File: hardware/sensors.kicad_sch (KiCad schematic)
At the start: 15 parts, among them U3 LIS3DH, U4 IMP23ABSU, U5 TMP102xxDRL, U6 VCNL_4020

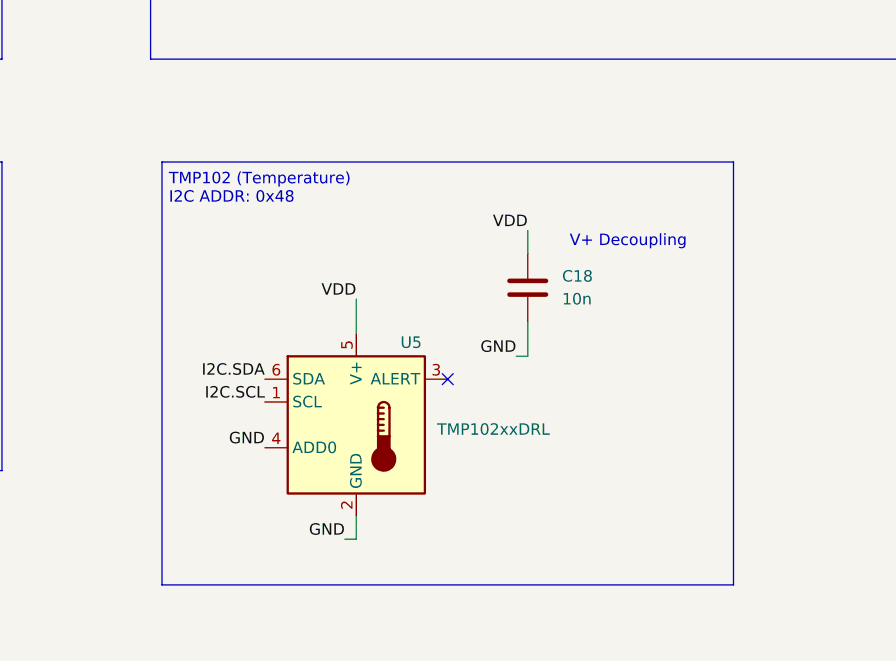
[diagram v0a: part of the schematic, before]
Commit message: [Hardware] Remove tmp102
No longer using the tmp102 temperature sensor, so remove it from the board.
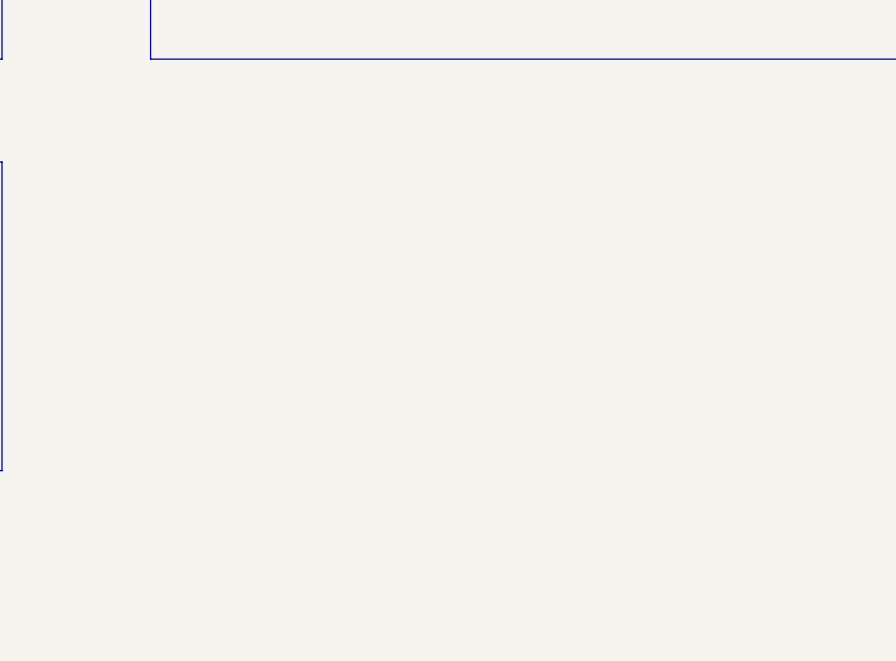
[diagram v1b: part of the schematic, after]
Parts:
- removed C18: 10n, Capacitor_SMD:C_0603_1608Metric_Pad1.08x0.95mm_HandSolder, symbol Device:C
- removed U5: TMP102xxDRL, Package_TO_SOT_SMD:SOT-563, symbol Sensor_Temperature:TMP102xxDRL
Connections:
- no-connect marks 6 -> 5
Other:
- note removed: "TMP102 (Temperature) I2C ADDR: 0x48"
- note removed: "V+ Decoupling"

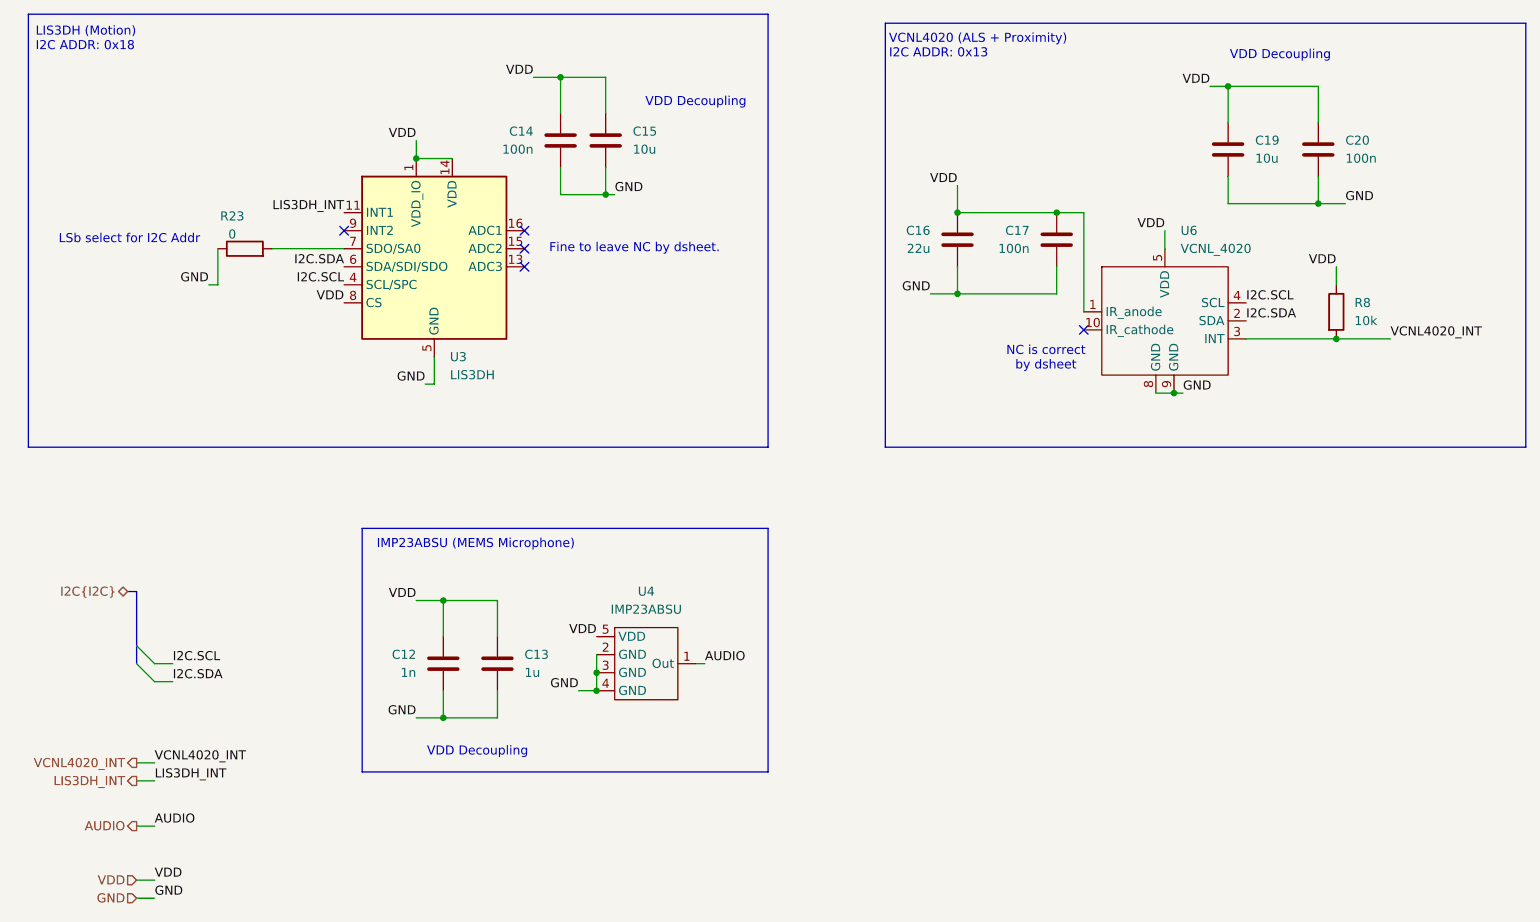
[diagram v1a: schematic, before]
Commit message: [Hardware] Replace LISDH Motion Sensor with LSM6DSM
Change motion sensor to an accelerometer + gyro unit. Route the second interrupt line to the STM32.
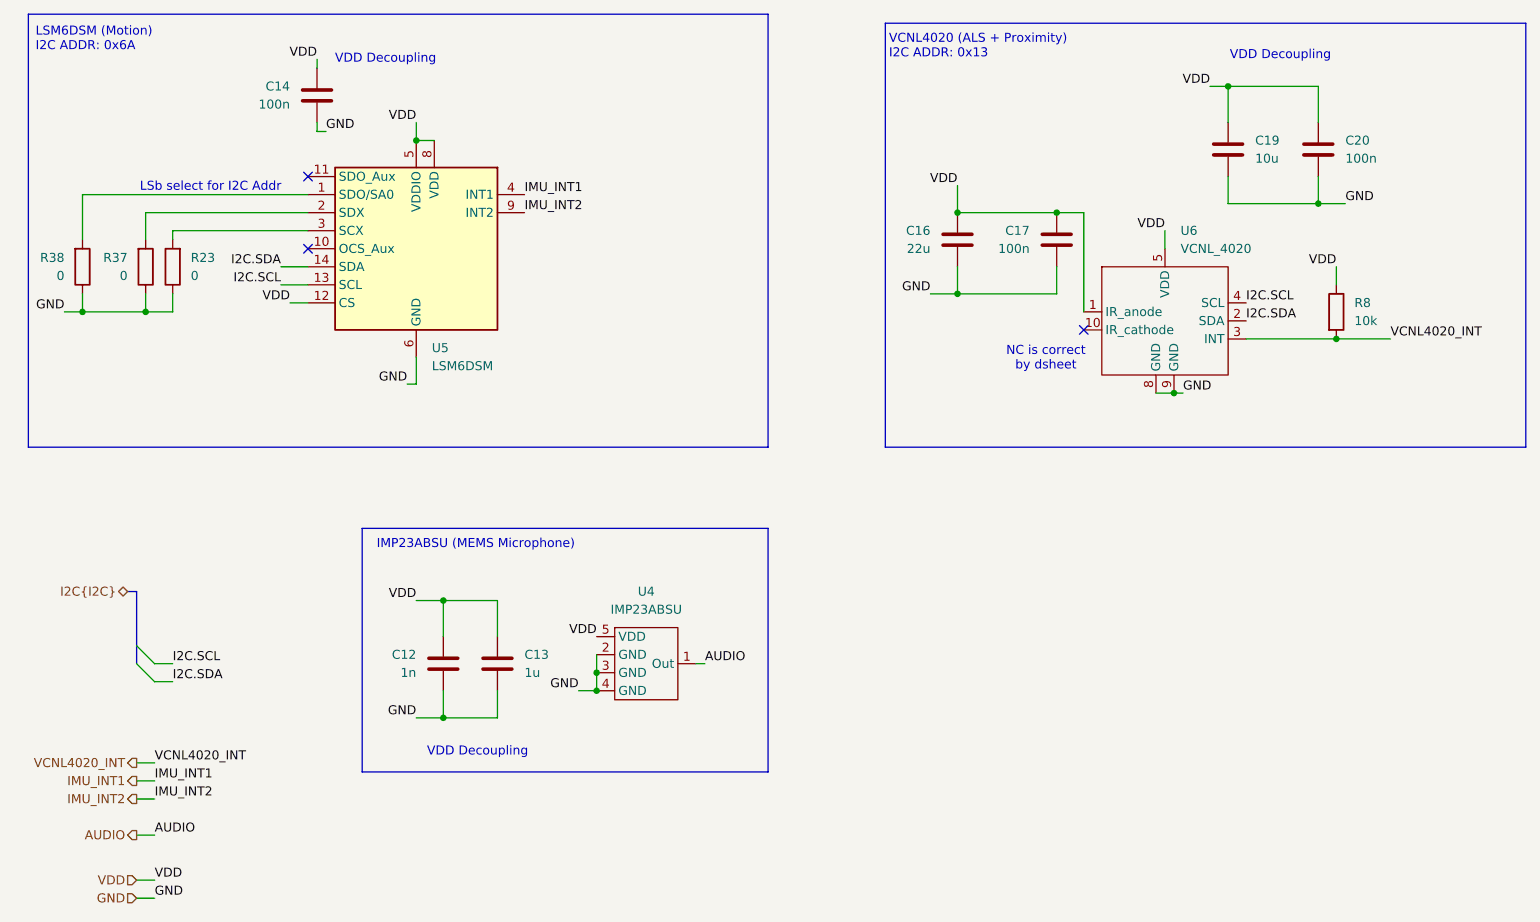
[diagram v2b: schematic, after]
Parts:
- removed C15: 10u, Capacitor_SMD:C_0603_1608Metric_Pad1.08x0.95mm_HandSolder, symbol Device:C
- removed U3: LIS3DH, Package_LGA:LGA-16_3x3mm_P0.5mm_LayoutBorder3x5y, symbol Sensor_Motion:LIS3DH
- added R37, R38: 0, Resistor_SMD:R_0603_1608Metric_Pad0.98x0.95mm_HandSolder, symbol Device:R
- added U5: LSM6DSM, Package_LGA:LGA-14_3x2.5mm_P0.5mm_LayoutBorder3x4y, symbol Sensor_Motion:LSM6DSM
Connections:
- net GND: now also R37.1, R38.1, U5.6 (GND), U5.7 (GND)
- net I2C.SCL: now also U5.13 (SCL)
- net I2C.SDA: now also U5.14 (SDA)
- net VDD: now also U5.12 (CS), U5.5 (VDDIO), U5.8 (VDD)
- net at R23.2: now also U5.3 (SCX)
- new net: R38.2, U5.1 (SDO/SA0)
- new net: R37.2, U5.2 (SDX)
- new net IMU_INT1: U5.4 (INT1)
- new net IMU_INT2: U5.9 (INT2)
- no-connect marks 5 -> 3
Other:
- note added: "LSM6DSM (Motion) I2C ADDR: 0x6A"
- note removed: "Fine to leave NC by dsheet."
- note removed: "LIS3DH (Motion) I2C ADDR: 0x18"
- moved on the sheet: C14

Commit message: Change many passives to 0402 and assign part numbers
Incorporate 0402 parts where possible
Assign Manufacturer Part Numbers to parts where possible
Update layout for the new passive sizes
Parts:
- C12: footprint Capacitor_SMD:C_0603_1608Metric_Pad1.08x0.95mm_HandSolder -> Capacitor_SMD:C_0402_1005Metric; MPN (none) -> C0402C102K4RACTU
- C13: MPN (none) -> CL05A105KO5NNNC
- C14, C17, C20: footprint Capacitor_SMD:C_0603_1608Metric_Pad1.08x0.95mm_HandSolder -> Capacitor_SMD:C_0402_1005Metric; MPN (none) -> CL05A104KA5NNNC
- C16: MPN (none) -> CL10A226MO7JZNC
- C19: MPN (none) -> CL10A106MQ8NNNC
- R23, R37, R38: footprint Resistor_SMD:R_0603_1608Metric_Pad0.98x0.95mm_HandSolder -> Resistor_SMD:R_0402_1005Metric; MPN (none) -> RC0402JR-070RL
- R8: footprint Resistor_SMD:R_0603_1608Metric_Pad0.98x0.95mm_HandSolder -> Resistor_SMD:R_0402_1005Metric; MPN (none) -> RC0402FR-0710KL
- U4: MPN (none) -> IMP23ABSUTR
- U5: MPN (none) -> LSM6DSMTR
- U6: MPN (none) -> VCNL4020-GS08
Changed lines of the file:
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@@
 			)
 		)
-		(property "Footprint" "Capacitor_SMD:C_0603_1608Metric_Pad1.08x0.95mm_HandSolder"
+		(property "Footprint" "Capacitor_SMD:C_0402_1005Metric"
 			(at 175.5648 52.07 0)
 			(effects
@@
 		)
 		(property "Description" "Unpolarized capacitor"
+			(at 176.53 48.26 0)
+			(effects
+				(font
+					(size 1.27 1.27)
+				)
+				(hide yes)
+			)
+		)
+		(property "MPN" "CL05A104KA5NNNC"
 			(at 176.53 48.26 0)
 			(effects
@@
 			)
 		)
-		(property "Footprint" "Resistor_SMD:R_0603_1608Metric_Pad0.98x0.95mm_HandSolder"
+		(property "Footprint" "Resistor_SMD:R_0402_1005Metric"
 			(at 53.848 52.07 90)
 			(effects
@@
 		)
 		(property "Description" "Resistor"
+			(at 52.07 52.07 0)
+			(effects
+				(font
+					(size 1.27 1.27)
+				)
+				(hide yes)
+			)
+		)
+		(property "MPN" "RC0402JR-070RL"
 			(at 52.07 52.07 0)
 			(effects
@@
 			)
 		)
-		(property "Footprint" "Capacitor_SMD:C_0603_1608Metric_Pad1.08x0.95mm_HandSolder"
+		(property "Footprint" "Capacitor_SMD:C_0402_1005Metric"
 			(at 71.4248 31.75 0)
 			(effects
@@
 		)
 		(property "Description" "Unpolarized capacitor"
+			(at 72.39 27.94 0)
+			(effects
+				(font
+					(size 1.27 1.27)
+				)
+				(hide yes)
+			)
+		)
+		(property "MPN" "CL05A104KA5NNNC"
 			(at 72.39 27.94 0)
 			(effects
@@
 			)
 		)
+		(property "MPN" "CL10A106MQ8NNNC"
+			(at 200.66 35.56 0)
+			(effects
+				(font
+					(size 1.27 1.27)
+				)
+				(hide yes)
+			)
+		)
 		(pin "2"
 		)
@@
 			)
 		)
-		(property "Footprint" "Resistor_SMD:R_0603_1608Metric_Pad0.98x0.95mm_HandSolder"
+		(property "Footprint" "Resistor_SMD:R_0402_1005Metric"
 			(at 37.592 52.07 90)
 			(effects
@@
 			)
 		)
+		(property "MPN" "RC0402JR-070RL"
+			(at 39.37 52.07 0)
+			(effects
+				(font
+					(size 1.27 1.27)
+				)
+				(hide yes)
+			)
+		)
 		(pin "1"
 		)
@@
 			)
 		)
-		(property "Footprint" "Capacitor_SMD:C_0603_1608Metric_Pad1.08x0.95mm_HandSolder"
+		(property "Footprint" "Capacitor_SMD:C_0402_1005Metric"
 			(at 91.1352 111.76 0)
 			(effects
@@
 		)
 		(property "Description" "Unpolarized capacitor"
+			(at 90.17 107.95 0)
+			(effects
+				(font
+					(size 1.27 1.27)
+				)
+				(hide yes)
+			)
+		)
+		(property "MPN" "C0402C102K4RACTU"
 			(at 90.17 107.95 0)
 			(effects
@@
 			)
 		)
+		(property "MPN" "LSM6DSMTR"
+			(at 86.36 49.53 0)
+			(effects
+				(font
+					(size 1.27 1.27)
+				)
+				(hide yes)
+			)
+		)
 		(pin "7"
 		)
@@
 			)
 		)
+		(property "MPN" "CL05A105KO5NNNC"
+			(at 97.79 107.95 0)
+			(effects
+				(font
+					(size 1.27 1.27)
+				)
+				(hide yes)
+			)
+		)
 		(pin "2"
 		)
@@
 			)
 		)
-		(property "Footprint" "Capacitor_SMD:C_0603_1608Metric_Pad1.08x0.95mm_HandSolder"
+		(property "Footprint" "Capacitor_SMD:C_0402_1005Metric"
 			(at 214.3252 39.37 0)
 			(effects
@@
 		)
 		(property "Description" "Unpolarized capacitor"
+			(at 213.36 35.56 0)
+			(effects
+				(font
+					(size 1.27 1.27)
+				)
+				(hide yes)
+			)
+		)
+		(property "MPN" "CL05A104KA5NNNC"
 			(at 213.36 35.56 0)
 			(effects
@@
 			)
 		)
-		(property "Footprint" "Resistor_SMD:R_0603_1608Metric_Pad0.98x0.95mm_HandSolder"
+		(property "Footprint" "Resistor_SMD:R_0402_1005Metric"
 			(at 46.482 52.07 90)
 			(effects
@@
 		)
 		(property "Description" "Resistor"
+			(at 48.26 52.07 0)
+			(effects
+				(font
+					(size 1.27 1.27)
+				)
+				(hide yes)
+			)
+		)
+		(property "MPN" "RC0402JR-070RL"
 			(at 48.26 52.07 0)
 			(effects
@@
 			)
 		)
+		(property "MPN" "IMP23ABSUTR"
+			(at 119.38 107.95 0)
+			(effects
+				(font
+					(size 1.27 1.27)
+				)
+				(hide yes)
+			)
+		)
 		(pin "1"
 		)
@@
 			)
 		)
+		(property "MPN" "CL10A226MO7JZNC"
+			(at 162.56 48.26 0)
+			(effects
+				(font
+					(size 1.27 1.27)
+				)
+				(hide yes)
+			)
+		)
 		(pin "2"
 		)
@@
 			)
 		)
-		(property "Footprint" "Resistor_SMD:R_0603_1608Metric_Pad0.98x0.95mm_HandSolder"
+		(property "Footprint" "Resistor_SMD:R_0402_1005Metric"
 			(at 214.122 58.42 90)
 			(effects
@@
 		)
 		(property "Description" "Resistor"
+			(at 215.9 58.42 0)
+			(effects
+				(font
+					(size 1.27 1.27)
+				)
+				(hide yes)
+			)
+		)
+		(property "MPN" "RC0402FR-0710KL"
 			(at 215.9 58.42 0)
 			(effects
@@
 			(at 191.77 57.15 0)
 			(effects
+				(font
+					(size 1.27 1.27)
+				)
+				(hide yes)
+			)
+		)
+		(property "MPN" "VCNL4020-GS08"
+			(at 191.77 57.15 0)
+			(effects
